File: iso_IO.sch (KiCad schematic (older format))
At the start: 25 parts, among them J9 AVR-ISP-6, U10 AM26LV32xD, U11 ADuM120N, U12 ADuM120N, U13 SFH617A-1, U9 ATtiny13A-SU

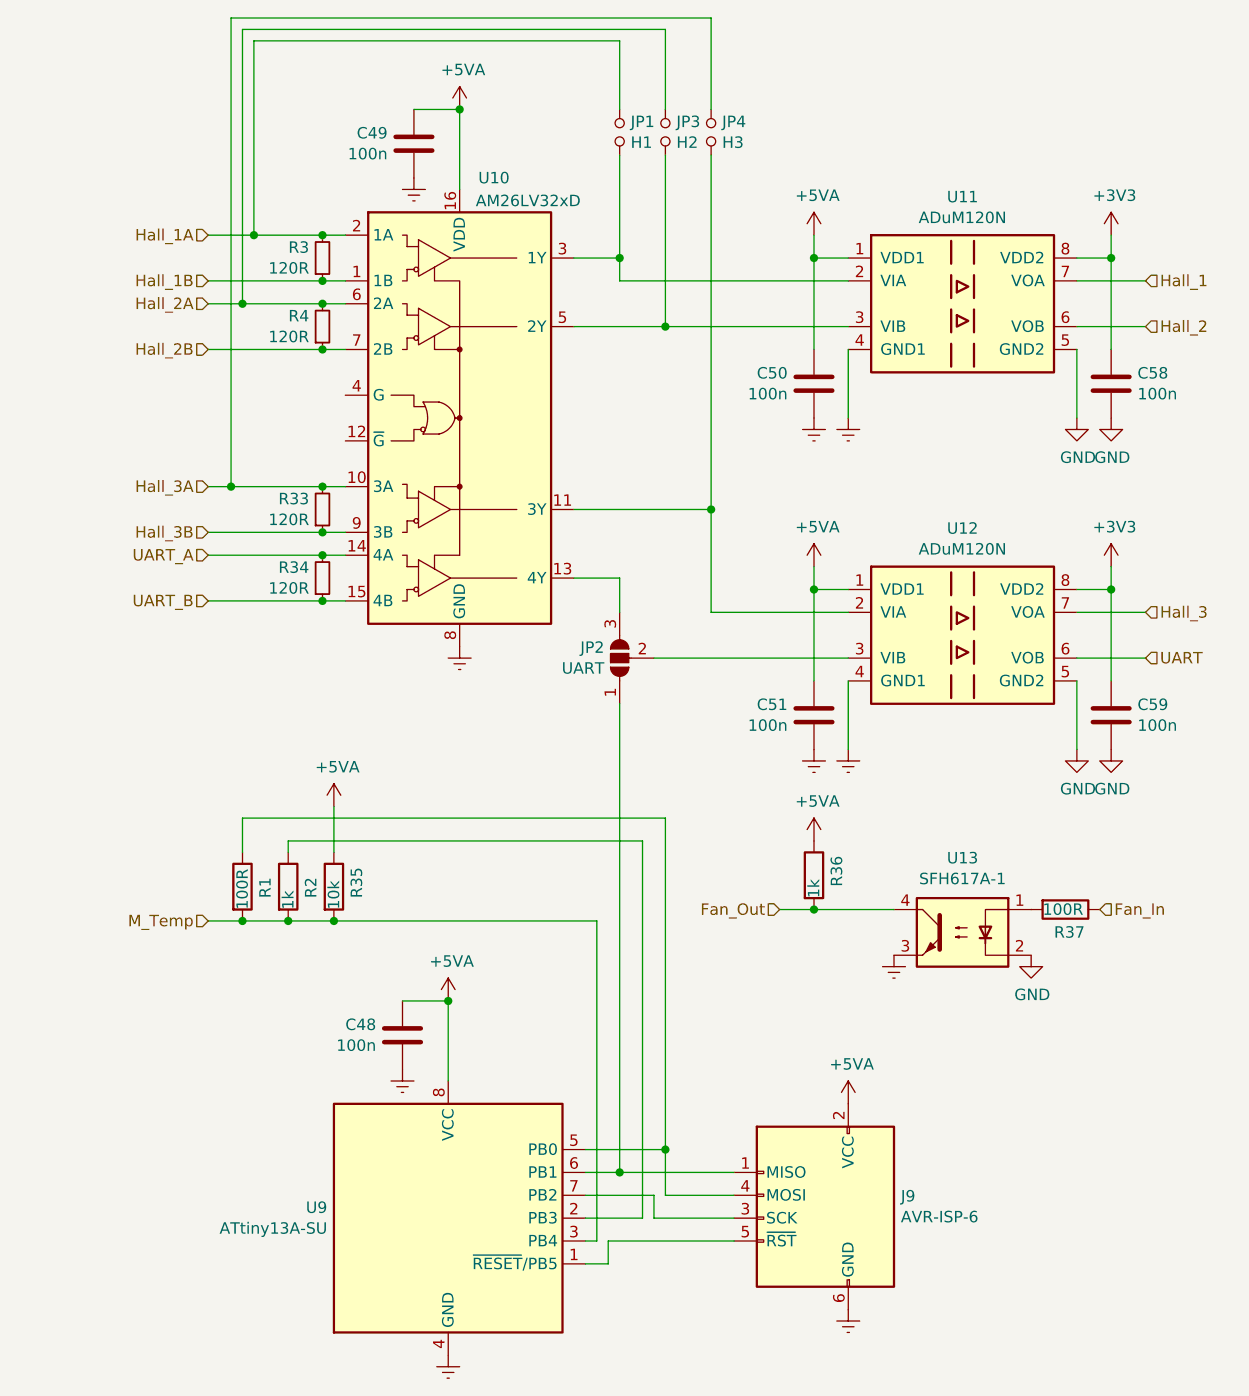
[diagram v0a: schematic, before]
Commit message: - added high power capabilities to fan output - moved CAN isolator - connected fan output to PB10 (TIM2_CH3)
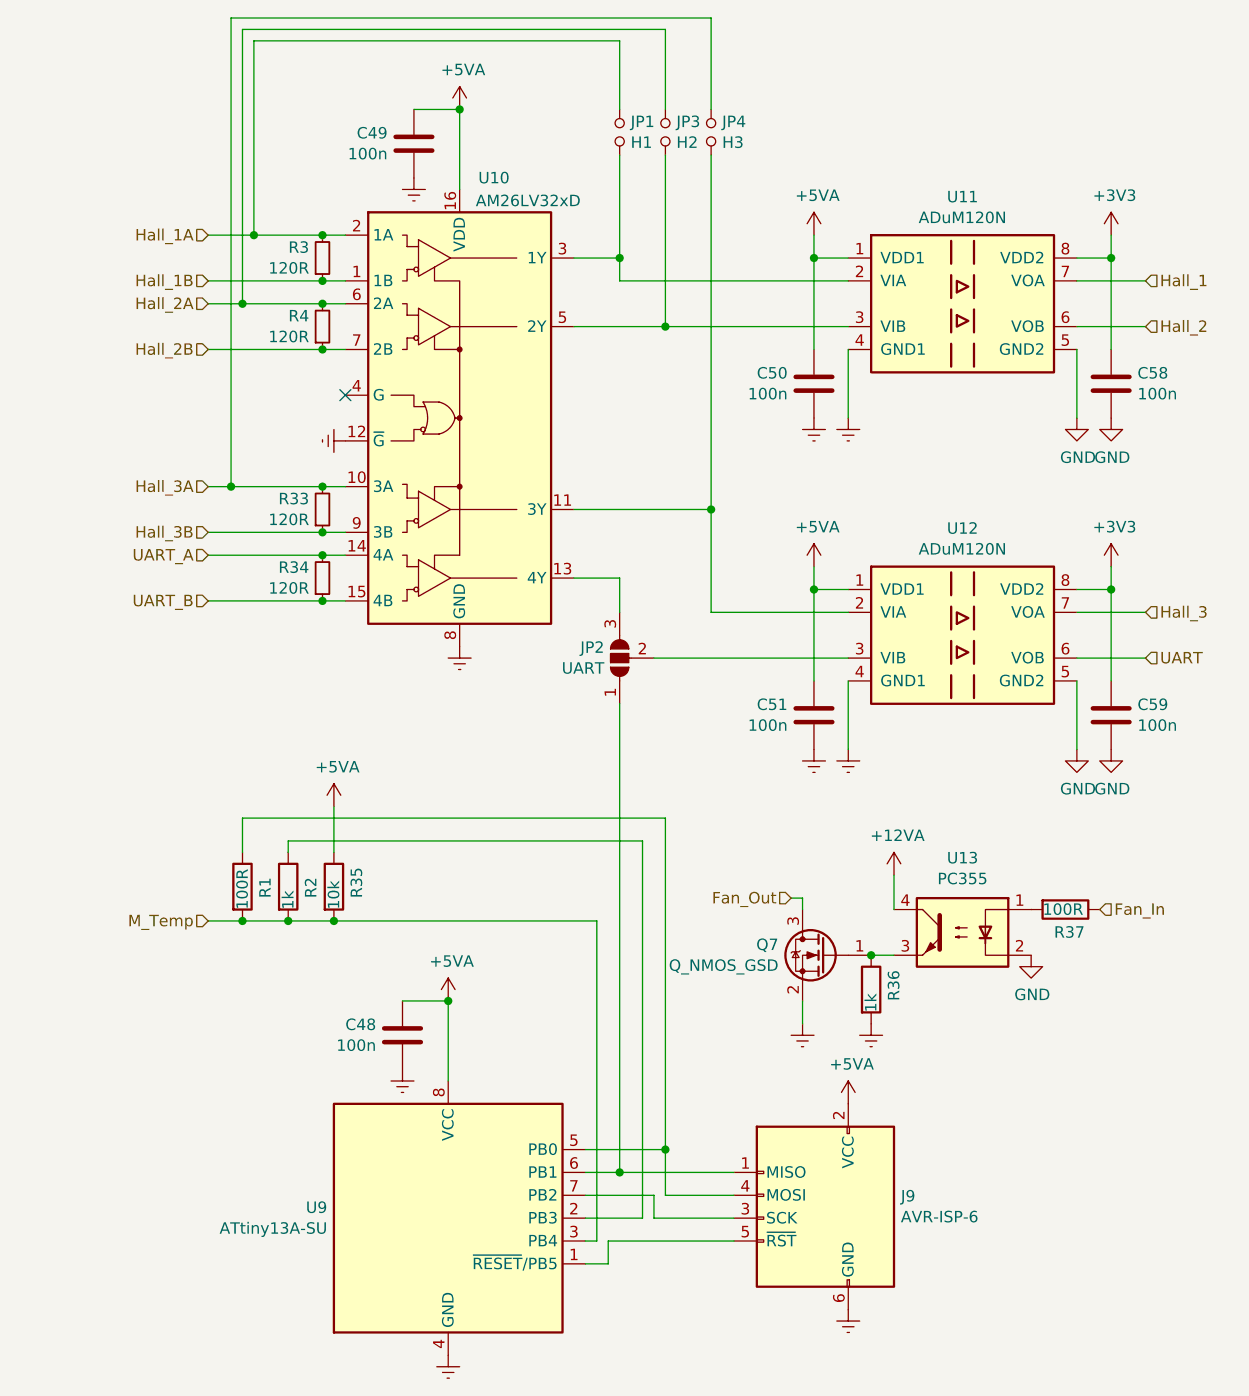
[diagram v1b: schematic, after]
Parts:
- added Q7: Q_NMOS_GSD, Package_TO_SOT_SMD:SOT-23, symbol Device:Q_NMOS_GSD
- U13: value SFH617A-1 -> PC355
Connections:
- net +5VA: no longer R36.1
- net Earth: now also R36.2, U10.12 (~G), Q7.2 (S); no longer U13.3
- net Fan_Out: now also Q7.3 (D); no longer R36.2, U13.4
- new net: Q7.1 (G), R36.1, U13.3
- new net +12VA: U13.4
- no-connect marks 0 -> 1
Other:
- moved on the sheet: R36
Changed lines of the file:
@@
 EESchema Schematic File Version 4
-LIBS:HSWR-cache
 EELAYER 30 0
 EELAYER END
@@
 Wire Wire Line
 	6100 1950 5800 1950
-Text HLabel 4500 4500 0    50   Input ~ 0
+Text HLabel 4550 4450 0    50   Input ~ 0
 Fan_Out
 $Comp
@@
 L Device:R R36
 U 1 1 5E612036
-P 4650 4350
-F 0 "R36" V 4750 4300 50  0000 L CNN
-F 1 "1k" V 4650 4250 50  0000 L CNN
-F 2 "Resistor_SMD:R_0805_2012Metric" V 4580 4350 50  0001 C CNN
-F 3 "~" H 4650 4350 50  0001 C CNN
-	1    4650 4350
-	1    0    0    -1
-$EndComp
-$Comp
-L power:+5VA #PWR0129
-U 1 1 5E612A16
-P 4650 4200
-F 0 "#PWR0129" H 4650 4050 50  0001 C CNN
-F 1 "+5VA" H 4665 4373 50  0000 C CNN
-F 2 "" H 4650 4200 50  0001 C CNN
-F 3 "" H 4650 4200 50  0001 C CNN
-	1    4650 4200
+P 4900 4850
+F 0 "R36" V 5000 4800 50  0000 L CNN
+F 1 "1k" V 4900 4750 50  0000 L CNN
+F 2 "Resistor_SMD:R_0805_2012Metric" V 4830 4850 50  0001 C CNN
+F 3 "~" H 4900 4850 50  0001 C CNN
+	1    4900 4850
 	1    0    0    -1
 $EndComp
@@
 P 5300 4600
 F 0 "U13" H 5300 4925 50  0000 C CNN
-F 1 "SFH617A-1" H 5300 4834 50  0000 C CNN
+F 1 "PC355" H 5300 4834 50  0000 C CNN
 F 2 "Package_SO:SO-4_4.4x4.3mm_P2.54mm" H 5100 4400 50  0001 L CIN
 F 3 "http://www.vishay.com/docs/83740/sfh617a.pdf" H 5300 4600 50  0001 L CNN
@@
 	1    0    0    -1
 $EndComp
-Wire Wire Line
-	4500 4500 4650 4500
-Connection ~ 4650 4500
-Wire Wire Line
-	4650 4500 5000 4500
 $Comp
 L power:Earth #PWR0137
 U 1 1 5E660775
-P 5000 4700
-F 0 "#PWR0137" H 5000 4450 50  0001 C CNN
-F 1 "Earth" H 5000 4550 50  0001 C CNN
-F 2 "" H 5000 4700 50  0001 C CNN
-F 3 "~" H 5000 4700 50  0001 C CNN
-	1    5000 4700
+P 4900 5000
+F 0 "#PWR0137" H 4900 4750 50  0001 C CNN
+F 1 "Earth" H 4900 4850 50  0001 C CNN
+F 2 "" H 4900 5000 50  0001 C CNN
+F 3 "~" H 4900 5000 50  0001 C CNN
+	1    4900 5000
 	1    0    0    -1
 $EndComp
@@
 $EndComp
 $Comp
-L power:Earth #PWR?
+L power:Earth #PWR0141
 U 1 1 5E816044
 P 4800 6250
-F 0 "#PWR?" H 4800 6000 50  0001 C CNN
+F 0 "#PWR0141" H 4800 6000 50  0001 C CNN
 F 1 "Earth" H 4800 6100 50  0001 C CNN
 F 2 "" H 4800 6250 50  0001 C CNN
@@
 	1    0    0    -1
 $EndComp
+$Comp
+L Device:Q_NMOS_GSD Q7
+U 1 1 5E5DDA98
+P 4700 4700
+F 0 "Q7" H 4905 4746 50  0000 L CNN
+F 1 "Q_NMOS_GSD" H 4905 4655 50  0000 L CNN
+F 2 "Package_TO_SOT_SMD:SOT-23" H 4900 4800 50  0001 C CNN
+F 3 "~" H 4700 4700 50  0001 C CNN
+	1    4700 4700
+	-1   0    0    -1
+$EndComp
+Wire Wire Line
+	5000 4700 4900 4700
+Connection ~ 4900 4700
+Wire Wire Line
+	5000 4350 5000 4500
+$Comp
+L power:Earth #PWR0143
+U 1 1 5E5EB989
+P 4600 5000
+F 0 "#PWR0143" H 4600 4750 50  0001 C CNN
+F 1 "Earth" H 4600 4850 50  0001 C CNN
+F 2 "" H 4600 5000 50  0001 C CNN
+F 3 "~" H 4600 5000 50  0001 C CNN
+	1    4600 5000
+	1    0    0    -1
+$EndComp
+Wire Wire Line
+	4600 4900 4600 5000
+Wire Wire Line
+	4550 4450 4600 4450
+Wire Wire Line
+	4600 4450 4600 4500
+$Comp
+L power:+12VA #PWR0129
+U 1 1 5E600A7D
+P 5000 4350
+F 0 "#PWR0129" H 5000 4200 50  0001 C CNN
+F 1 "+12VA" H 5015 4523 50  0000 C CNN
+F 2 "" H 5000 4350 50  0001 C CNN
+F 3 "" H 5000 4350 50  0001 C CNN
+	1    5000 4350
+	1    0    0    -1
+$EndComp
+NoConn ~ 2600 2250
+$Comp
+L power:Earth #PWR0146
+U 1 1 5E607E51
+P 2600 2450
+F 0 "#PWR0146" H 2600 2200 50  0001 C CNN
+F 1 "Earth" H 2600 2300 50  0001 C CNN
+F 2 "" H 2600 2450 50  0001 C CNN
+F 3 "~" H 2600 2450 50  0001 C CNN
+	1    2600 2450
+	0    1    1    0
+$EndComp
 $EndSCHEMATC

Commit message: - fixed ISP connector being mirrored - changed some footprints to get them 3D Models - added a preliminary BOM
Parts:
- J9: footprint Connector_PinSocket_2.54mm:PinSocket_2x03_P2.54mm_Vertical -> Connector_PinHeader_2.54mm:PinHeader_2x03_P2.54mm_Vertical
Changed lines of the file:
@@
 F 0 "J9" H 4370 5946 50  0000 R CNN
 F 1 "AVR-ISP-6" H 4370 5855 50  0000 R CNN
-F 2 "Connector_PinSocket_2.54mm:PinSocket_2x03_P2.54mm_Vertical" V 4450 5900 50  0001 C CNN
+F 2 "Connector_PinHeader_2.54mm:PinHeader_2x03_P2.54mm_Vertical" V 4450 5900 50  0001 C CNN
 F 3 " ~" H 3425 5300 50  0001 C CNN
 	1    4700 5850

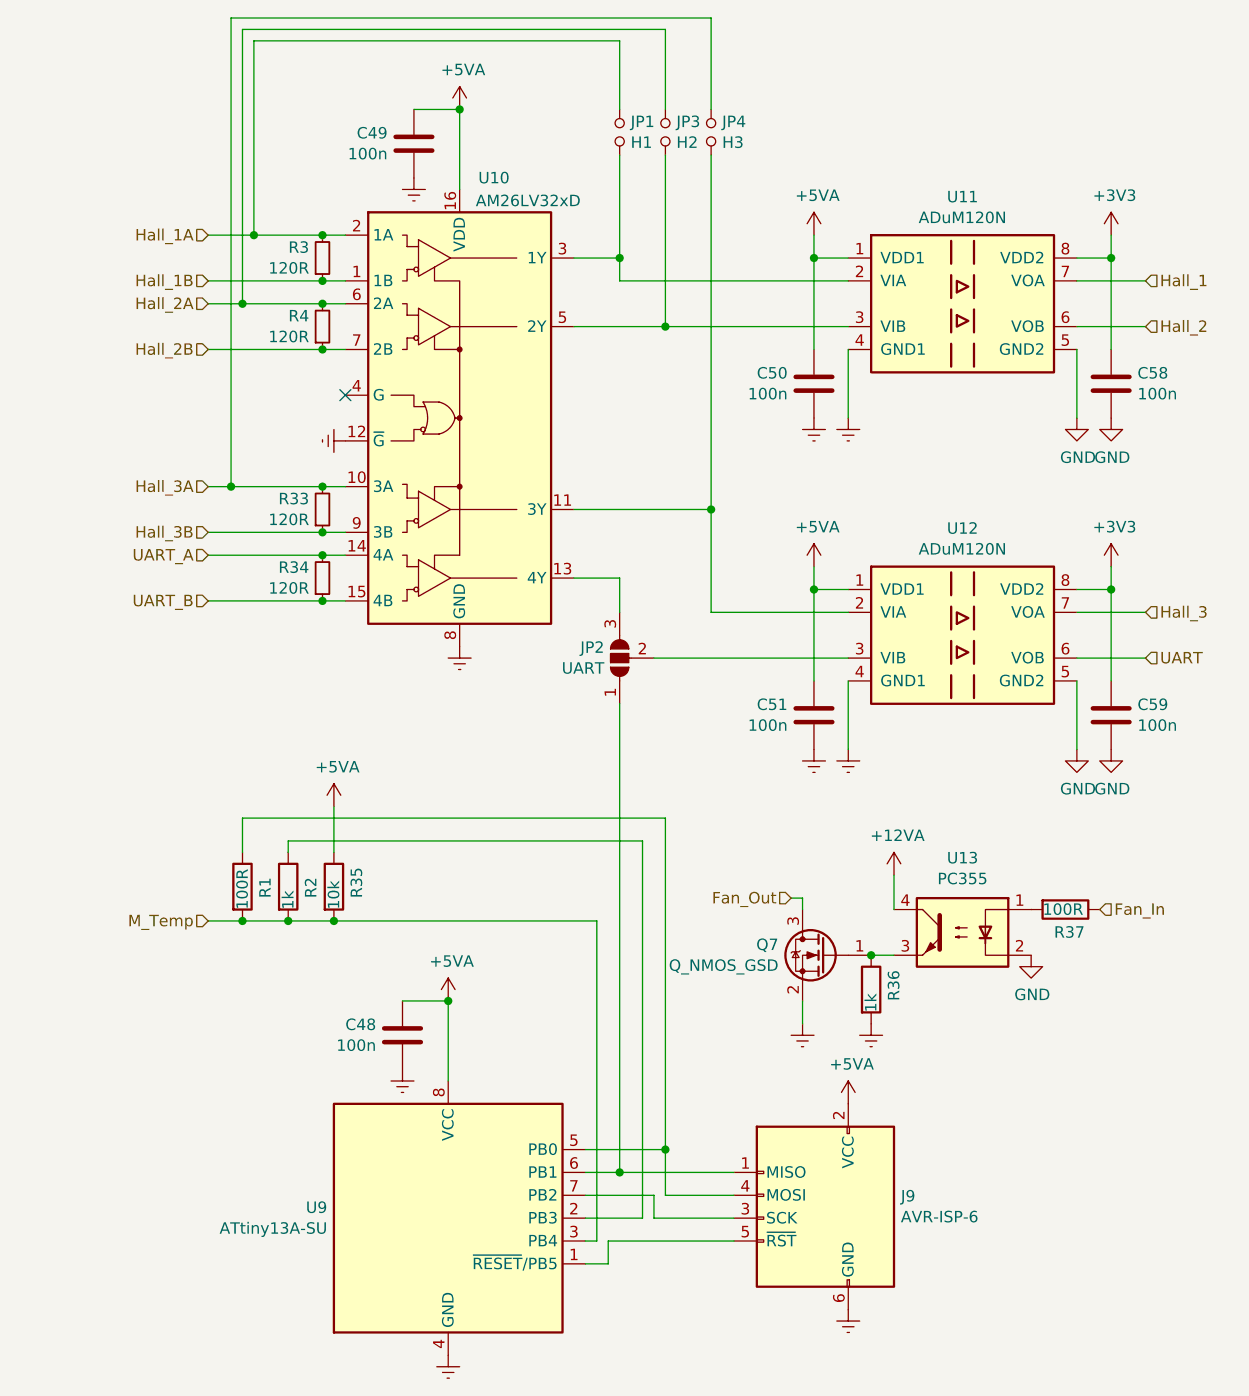
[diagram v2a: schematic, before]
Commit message: - enlarged isolated island - bigger package for fan MOSFET - added 12V input protection - added U_DC sensing filter - added M_temp input filter - added reset pin decoupling for AVR - added HALL pull-ups - added TRI state selector jumper for buffer - removed UART selector jumper (AVR will check and switch to TRI state if needed)
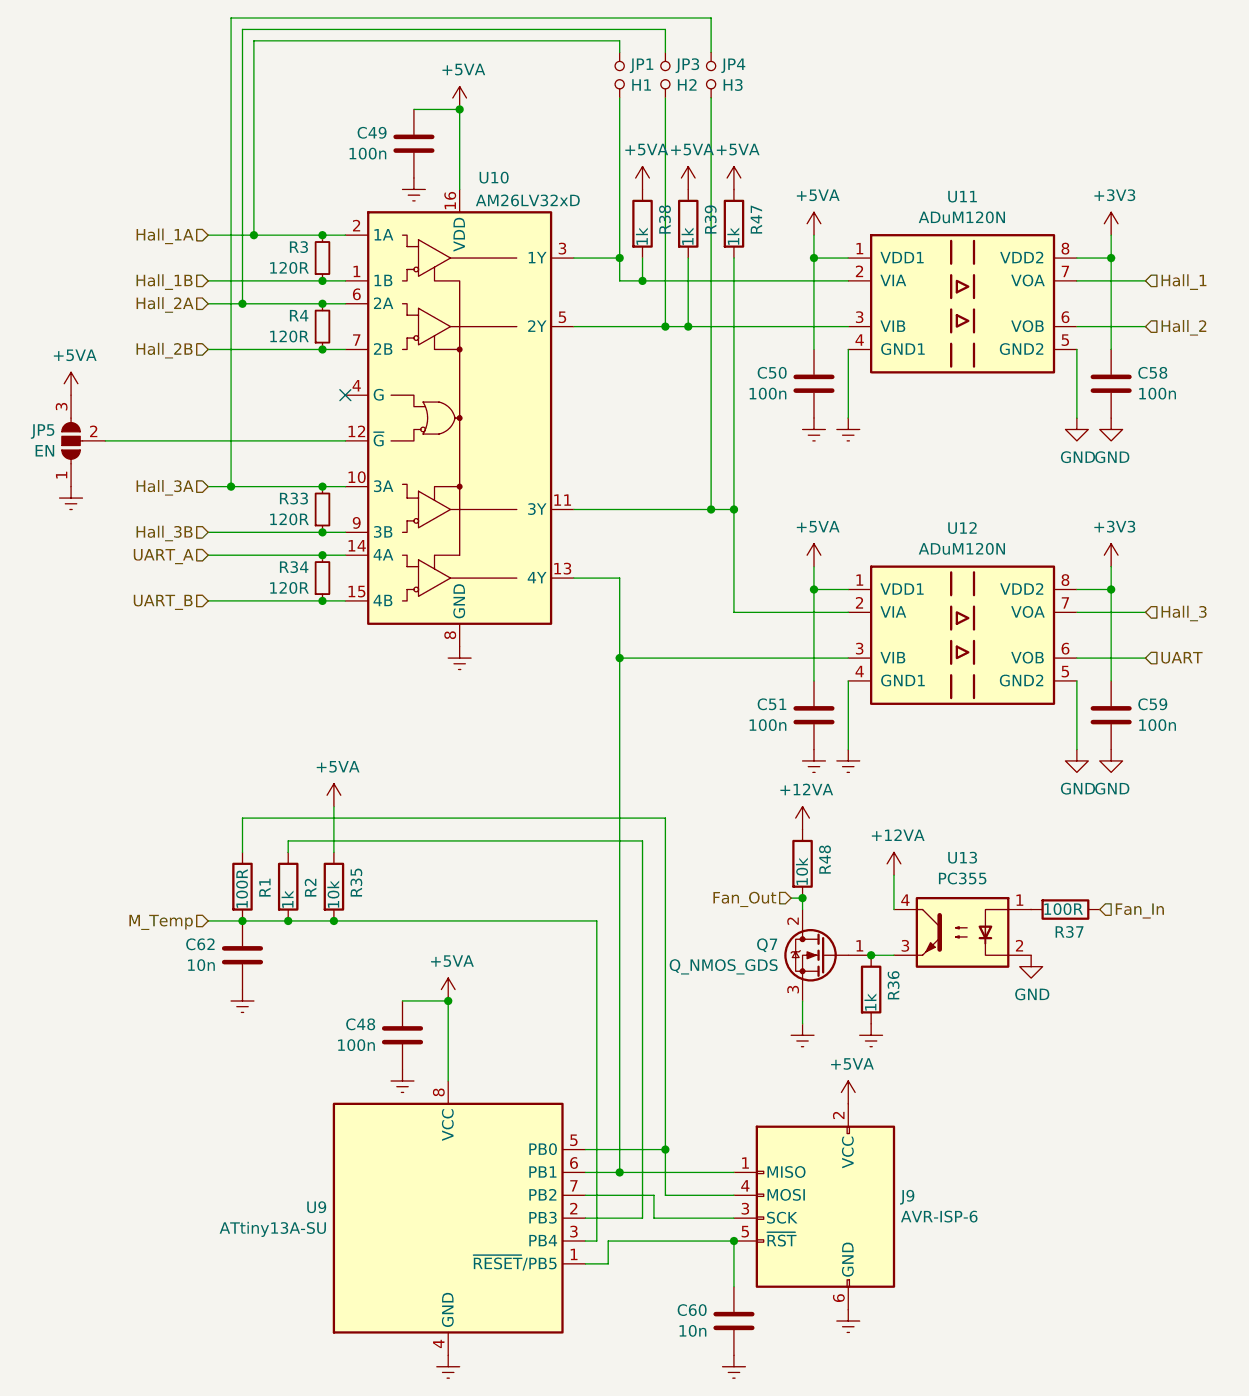
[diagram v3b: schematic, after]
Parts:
- removed JP2: UART, Jumper:SolderJumper-3_P2.0mm_Open_TrianglePad1.0x1.5mm, symbol Jumper:SolderJumper_3_Open
- removed Q7: Q_NMOS_GSD, Package_TO_SOT_SMD:SOT-23, symbol Device:Q_NMOS_GSD
- added C60, C62: 10n, Capacitor_SMD:C_0805_2012Metric, symbol Device:C
- added JP5: EN, Jumper:SolderJumper-3_P2.0mm_Open_TrianglePad1.0x1.5mm, symbol Jumper:SolderJumper_3_Open
- added Q7: Q_NMOS_GDS, Package_TO_SOT_SMD:SOT-223-3_TabPin2, symbol Device:Q_NMOS_GDS
- added R38, R39, R47: 1k, Resistor_SMD:R_0805_2012Metric, symbol Device:R
- added R48: 10k, Resistor_SMD:R_0805_2012Metric, symbol Device:R
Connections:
- net +12VA: now also R48.1
- net +5VA: now also JP5.3 (B), R38.1, R39.1, R47.1
- net Earth: now also C60.2, C62.2, JP5.1 (A), Q7.3 (S); no longer U10.12 (~G)
- net Fan_Out: now also Q7.2 (D), R48.2
- net M_Temp: now also C62.1
- net at JP1.2, U10.3 (1Y), U11.2 (VIA): now also R38.2
- net at JP3.2, U10.5 (2Y), U11.3 (VIB): now also R39.2
- net at R36.1, U13.3: now also Q7.1 (G)
- net at JP4.2, U10.11 (3Y), U12.2 (VIA): now also R47.2
- net at U10.13 (4Y): now also J9.1 (MISO), U12.3 (VIB), U9.6 (PB1)
- net at J9.5 (~RST), U9.1 (~RESET~/PB5): now also C60.1
- new net: JP5.2 (C), U10.12 (~G)
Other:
- moved on the sheet: JP1, JP3, JP4
